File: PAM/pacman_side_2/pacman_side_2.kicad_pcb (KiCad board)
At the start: 2 copper layers, 144.3 x 139.4 mm, 23 parts, among them J1 Conn_01x08, J2 Conn_01x04, J3 Conn_01x01, J4 Conn_01x01, J5 Conn_01x01, J6 Conn_01x02, J9 JST PH, K1 G2RL, K2 G5V-1, K3 G5V-1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

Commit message: finish layout and labeling
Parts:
- added G***: LOGO, AERO_Footprints:AERO_Logo_10x4mm, F.Cu at (112.1, 121.2)
- added REF**: Symbol_HighVoltage_Type2_CopperTop_VerySmall, Symbol:Symbol_HighVoltage_Type2_CopperTop_VerySmall, F.Cu at (163.2, 112.5)
- moved J9 68.9 mm to (107.1, 84.8)
- moved J5 68.1 mm to (137.0, 120.9), turned to 180 degrees
- moved F3 66.9 mm to (103.4, 77.5)
- moved J2 66.9 mm to (95.0, 90.8)
- moved K3 66.9 mm to (98.0, 75.3)
- moved D3 66.9 mm to (126.8, 73.3)
- moved D4 66.9 mm to (114.8, 87.8)
- moved D5 66.9 mm to (121.8, 92.1)
- moved J3 66.9 mm to (176.1, 122.3)
- moved J6 66.9 mm to (117.3, 70.8)
- moved K1 66.9 mm to (143.2, 73.8)
- moved K2 66.9 mm to (112.2, 82.4)
- moved Q2 66.9 mm to (122.6, 83.0)
- moved J1 66.9 mm to (111.3, 111.1)
- moved F1 66.9 mm to (139.0, 85.3)
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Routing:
- net +12V: track 0.00 -> 114.5 mm
- net /BMS_FAN: track 0.00 -> 65.8 mm
- net /INT-: track 0.00 -> 48.5 mm
- net Net-(K1-Pad5): track 0.00 -> 42.9 mm
- net /INT+: track 0.00 -> 35.5 mm
- net /B+: track 0.00 -> 16.3 mm
- net Net-(D1-Pad2): track 0.00 -> 12.1 mm
- net /FAN_OUT: track 3.40 -> 14.8 mm
- net Net-(F1-Pad1): track 0.00 -> 10.9 mm
- net /BMS_CAN-: track 22.9 -> 31.8 mm
- net Net-(F2-Pad1): track 0.00 -> 7.87 mm
- net /BMS_CAN+: track 25.1 -> 31.8 mm
- net /AIR_B+: track 21.9 -> 18.7 mm
- net /AIR_B-: track 76.1 -> 73.4 mm
- net GND: vias 0 -> 3
- added copper zone on B.Cu, net GND
- added copper zone on F.Cu, net GND
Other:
- board size 144.3 x 139.4 mm -> 92.7 x 66 mm
- board text added: "+ -"
- board text added: "12V"
- board text added: "2A"
- board text added: "AIR B+"
- board text added: "AIR B-"
- board text added: "CAN+"
- board text added: "CAN-"
- board text added: "FAN"
- board text added: "GND"
- board text added: "Pack 2"

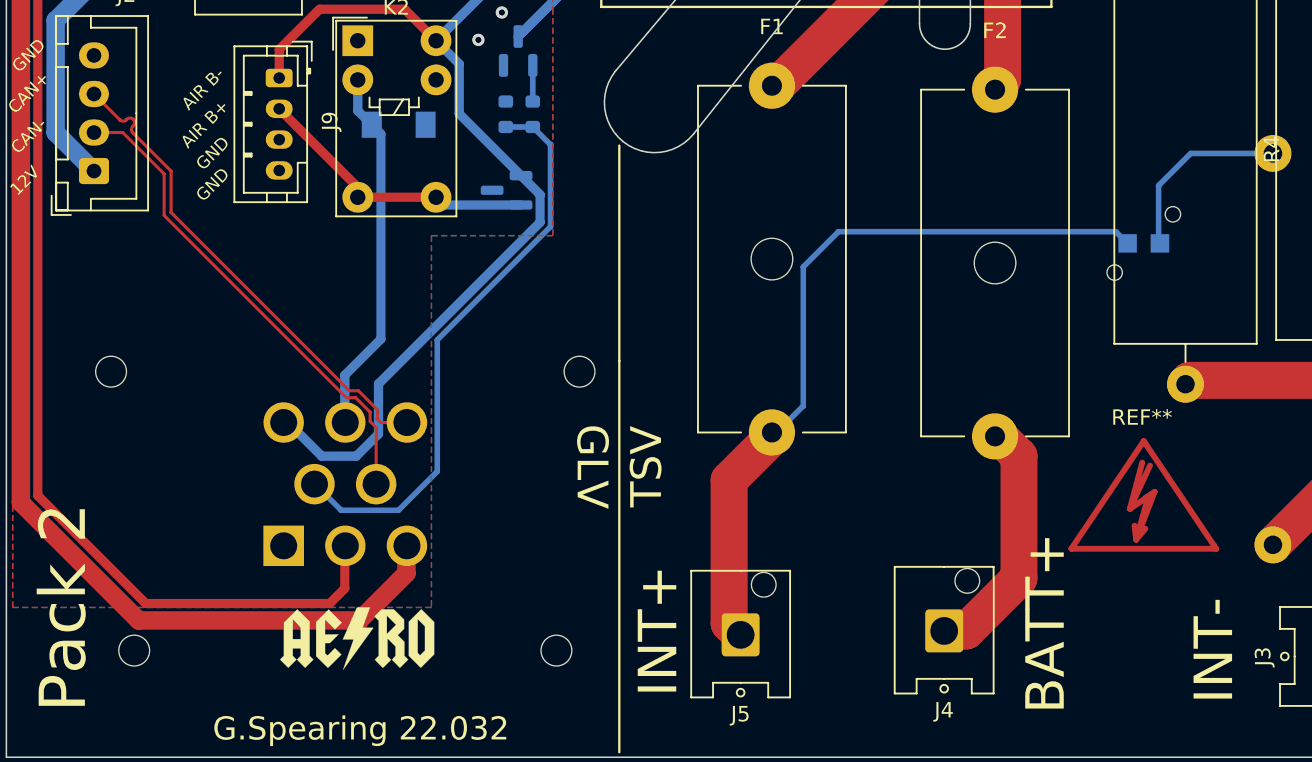
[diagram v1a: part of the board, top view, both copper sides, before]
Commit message: Adding CAN termination resistors
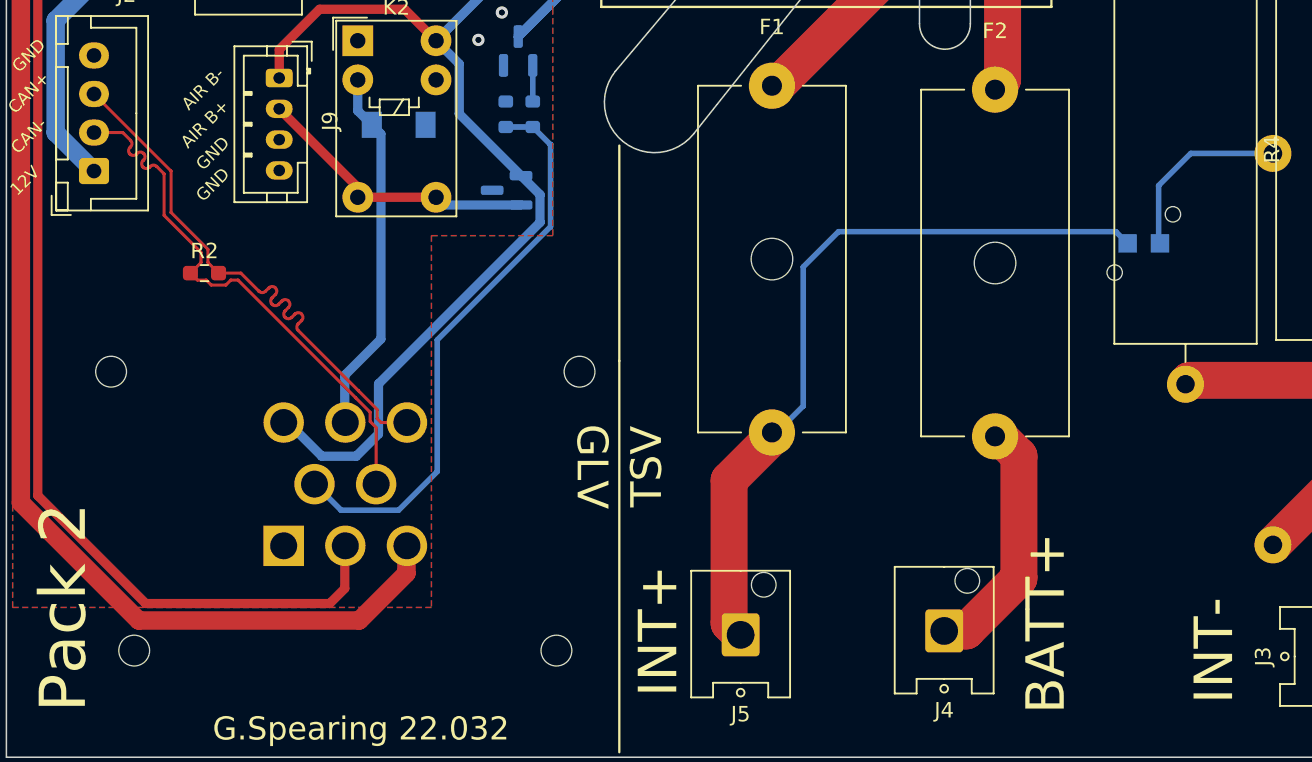
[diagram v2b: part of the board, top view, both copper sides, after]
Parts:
- removed G***: LOGO, AERO_Footprints:AERO_Logo_10x4mm
- removed REF**: Symbol_HighVoltage_Type2_CopperTop_VerySmall, Symbol:Symbol_HighVoltage_Type2_CopperTop_VerySmall
- added R2: 120, Resistor_SMD:R_0603_1608Metric_Pad0.98x0.95mm_HandSolder, F.Cu at (102.2, 97.4)
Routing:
- net /BMS_CAN+: track 31.8 -> 35.4 mm
- net /BMS_CAN-: track 31.8 -> 35.3 mm

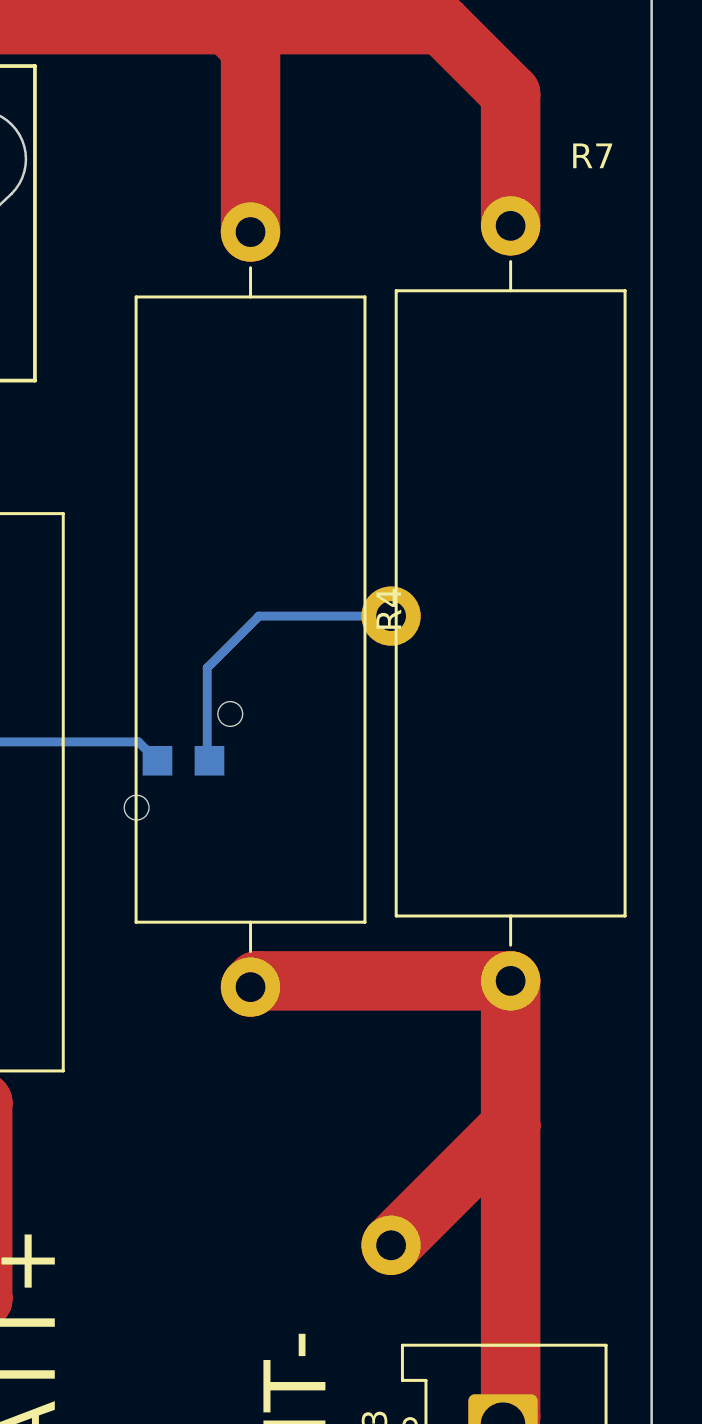
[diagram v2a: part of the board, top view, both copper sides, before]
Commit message: updating silkscreen objects
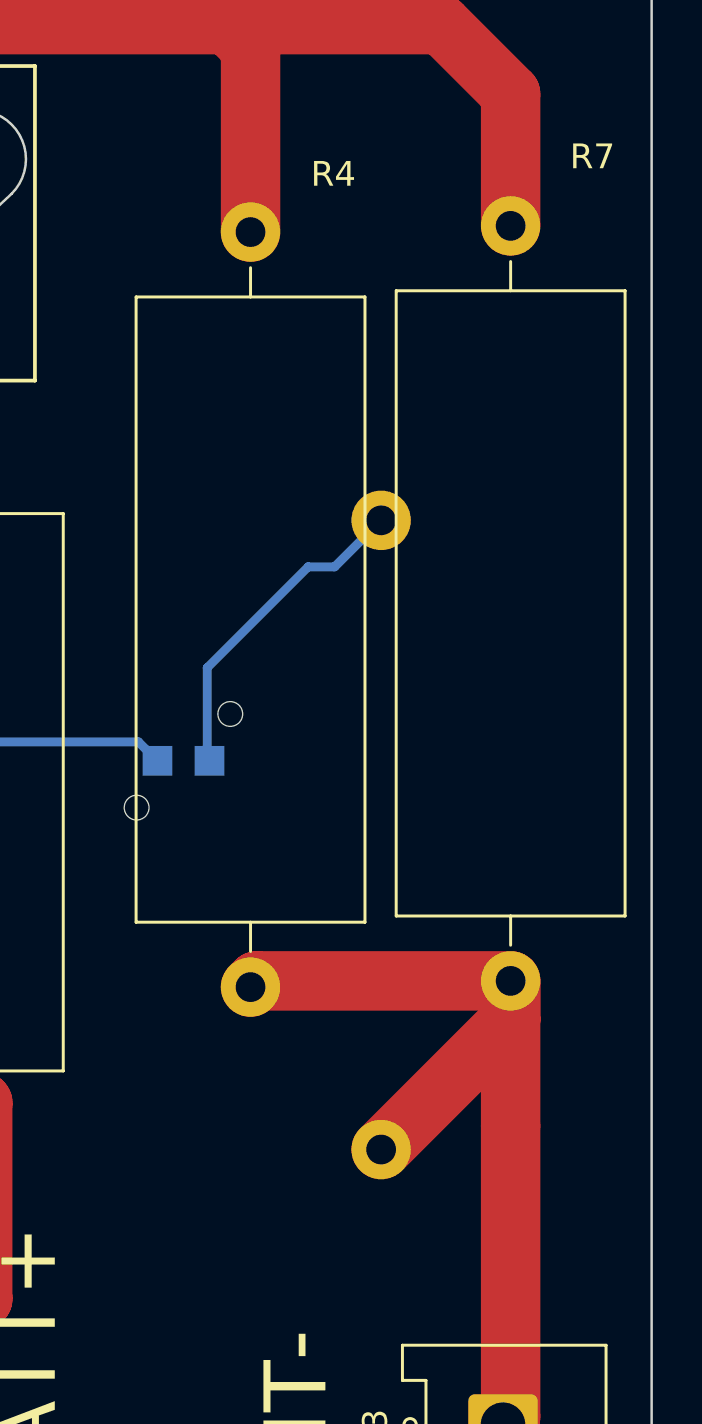
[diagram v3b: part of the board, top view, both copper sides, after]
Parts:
- moved R1 3.89 mm to (171.1, 111.2)
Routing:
- net /INT+: track 35.5 -> 37.6 mm
- net Net-(D1-Pad2): track 12.1 -> 13.3 mm
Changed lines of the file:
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@@
     (property "Sheetname" "")
     (attr through_hole)
-    (fp_text reference "R4" (at 15.24 -5.62 90) (layer "F.SilkS")
+    (fp_text reference "R4" (at -2.3328 -3.3418 180) (layer "F.SilkS")
       (effects (font (size 1 1) (thickness 0.15)))
     )
@@
   )
   (footprint "Resistor_THT:R_Axial_DIN0414_L11.9mm_D4.5mm_P25.40mm_Horizontal" (layer "B.Cu")
-    (at 171.547 115.067 90)
+    (at 171.1452 111.2012 90)
     (descr "Resistor, Axial_DIN0414 series, Axial, Horizontal, pin pitch=25.4mm, 2W, length*diameter=11.9*4.5mm^2, http://www.vishay.com/docs/20128/wkxwrx.pdf")
     (tags "Resistor Axial_DIN0414 series Axial Horizontal pin pitch 25.4mm 2W length 11.9mm diameter 4.5mm")
@@
   (segment (start 162.115 95.509) (end 161.351479 94.745479) (width 0.36) (layer "B.Cu") (net 1))
   (segment (start 161.351479 94.745479) (end 143.354521 94.745479) (width 0.36) (layer "B.Cu") (net 1))
-  (segment (start 171.547 89.667) (end 166.213 89.667) (width 0.36) (layer "B.Cu") (net 2))
-  (segment (start 166.213 89.667) (end 164.125479 91.754521) (width 0.36) (layer "B.Cu") (net 2))
-  (segment (start 164.125479 95.419479) (end 164.215 95.509) (width 0.36) (layer "B.Cu") (net 2))
-  (segment (start 164.125479 91.754521) (end 164.125479 95.419479) (width 0.36) (layer "B.Cu") (net 2))
+  (segment (start 168.1988 87.6812) (end 168.1988 87.6808) (width 0.36) (layer "B.Cu") (net 2))
+  (segment (start 164.125479 91.754521) (end 168.1988 87.6812) (width 0.36) (layer "B.Cu") (net 2))
+  (segment (start 164.125479 95.419479) (end 164.125479 91.754521) (width 0.36) (layer "B.Cu") (net 2))
+  (segment (start 164.215 95.509) (end 164.125479 95.419479) (width 0.36) (layer "B.Cu") (net 2))
+  (segment (start 168.1988 87.6808) (end 169.2656 87.6808) (width 0.36) (layer "B.Cu") (net 2))
+  (segment (start 169.2656 87.6808) (end 171.1452 85.8012) (width 0.36) (layer "B.Cu") (net 2))
   (segment (start 127.02531 77.621) (end 130.5 77.621) (width 0.6) (layer "B.Cu") (net 3))
   (segment (start 122.565 82.08131) (end 127.02531 77.621) (width 0.6) (layer "B.Cu") (net 3))
@@
   (arc (start 107.018965 99.459581) (mid 106.806833 99.547449) (end 106.594701 99.459581) (width 0.2) (layer "F.Cu") (net 14))
   (segment (start 176.373 122.003) (end 176.065 122.311) (width 2.4) (layer "F.Cu") (net 15))
+  (segment (start 176.373 105.9734) (end 171.1452 111.2012) (width 2.4) (layer "F.Cu") (net 15))
   (segment (start 176.373 104.394) (end 166.123 104.394) (width 2.4) (layer "F.Cu") (net 15))
   (segment (start 166.123 104.394) (end 165.873 104.644) (width 2.4) (layer "F.Cu") (net 15))
   (segment (start 176.373 110.241) (end 176.373 122.003) (width 2.4) (layer "F.Cu") (net 15))
   (segment (start 176.373 104.394) (end 176.373 110.241) (width 2.4) (layer "F.Cu") (net 15))
-  (segment (start 176.373 110.241) (end 171.547 115.067) (width 2.4) (layer "F.Cu") (net 15))
+  (segment (start 176.373 104.394) (end 176.373 105.9734) (width 2.4) (layer "F.Cu") (net 15))
   (segment (start 165.873 66.721) (end 165.873 74.164) (width 2.4) (layer "F.Cu") (net 16))
   (segment (start 154.83 65.791) (end 164.943 65.791) (width 2.4) (layer "F.Cu") (net 16))

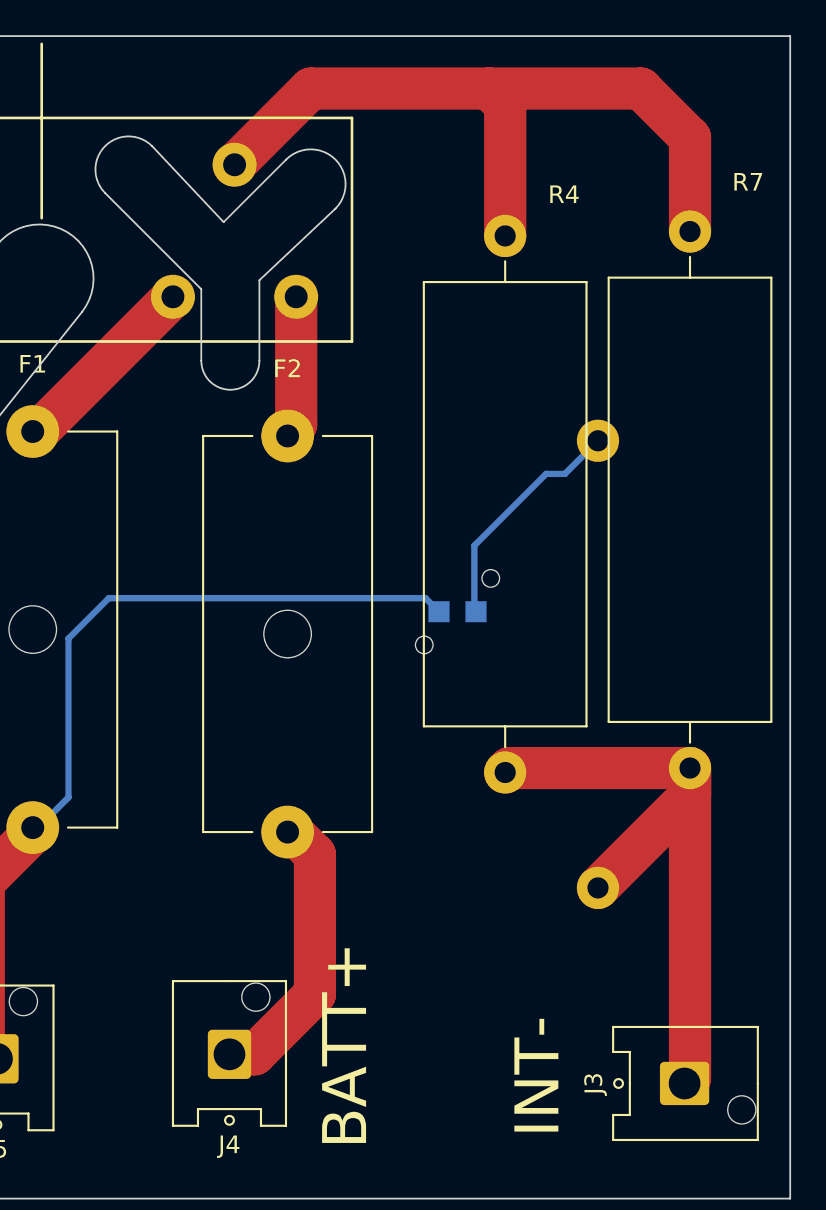
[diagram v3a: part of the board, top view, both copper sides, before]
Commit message: Major Review and Part Update
updating footprints, component values, layouts
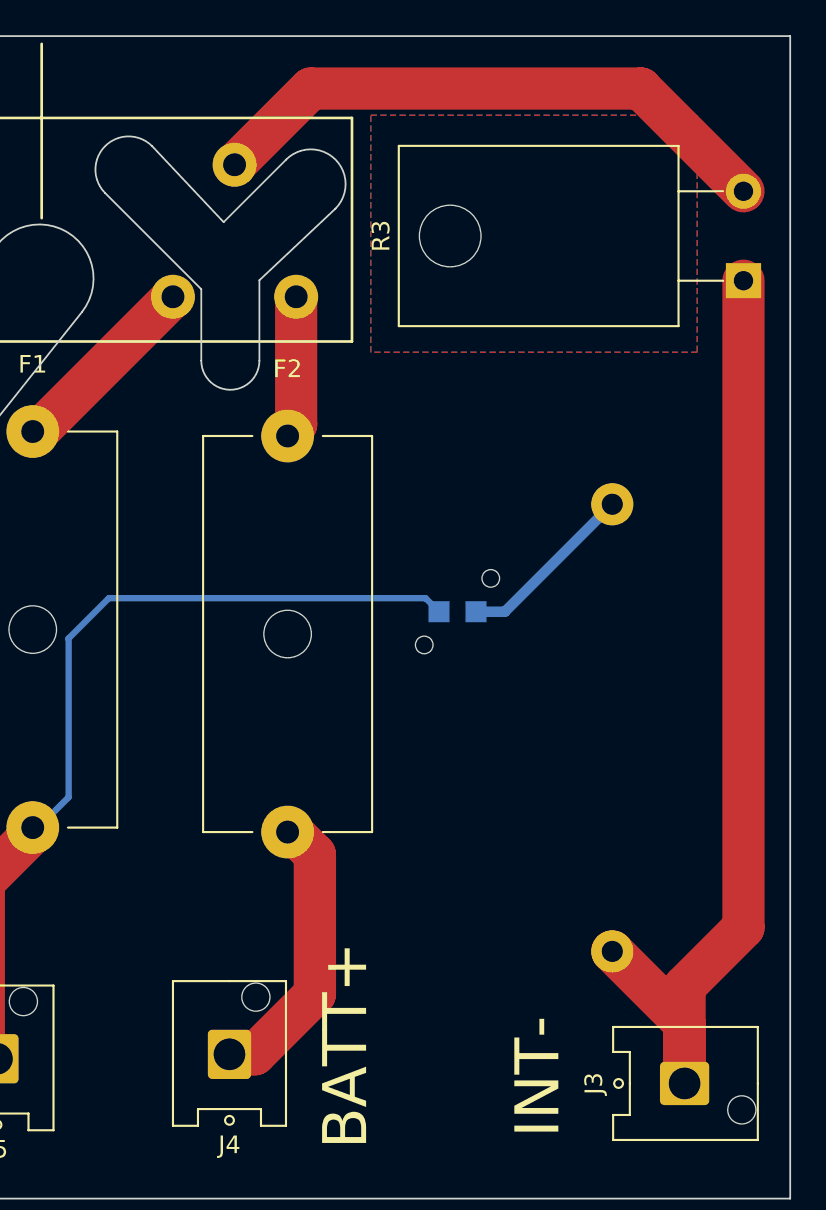
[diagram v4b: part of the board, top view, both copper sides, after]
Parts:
- removed R4, R7: 1k 7W, Resistor_THT:R_Axial_Power_L25.0mm_W9.0mm_P30.48mm
- added R3: 500, Package_TO_SOT_THT:TO-220-2_Horizontal_TabDown, F.Cu at (179.4, 76.7)
- moved R1 3.70 mm to (172.0, 114.8)
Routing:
- net /INT+: track 37.6 -> 56.2 mm
- net Net-(K1-Pad5): track 42.9 -> 33.1 mm
- net Net-(D1-Pad2): track 13.3 -> 10.3 mm
- added copper zone on B.Cu, net (none)
- added copper zone on F.Cu, net (none)

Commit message: touching up layout and making gerbers
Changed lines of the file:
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@@
       (outputformat 1)
       (mirror false)
-      (drillshape 1)
+      (drillshape 0)
       (scaleselection 1)
-      (outputdirectory "")
+      (outputdirectory "Pac2_Gerber/")
     )
   )
@@
     (fp_line (start 7.95 -1.7) (end -1.95 -1.7) (layer "F.Fab") (width 0.1))
     (fp_line (start 7.95 2.8) (end 7.95 -1.7) (layer "F.Fab") (width 0.1))
-    (pad "1" thru_hole roundrect locked (at 0 0 270) (size 1.2 1.75) (drill 0.75) (layers *.Cu *.Mask) (roundrect_rratio 0.208333)
+    (pad "1" thru_hole roundrect locked (at 0 0 270) (size 1.2 1.75) (drill 0.75) (layers *.Cu *.Mask) (roundrect_rratio 0.2083333333)
       (net 12 "/AIR_B-") (pinfunction "Pin_1") (pintype "passive"))
     (pad "2" thru_hole oval locked (at 2 0 270) (size 1.2 1.75) (drill 0.75) (layers *.Cu *.Mask)
@@
     (fp_line (start 0 -1.35) (end 0.625 -2.35) (layer "F.Fab") (width 0.1))
     (fp_line (start 9.95 -2.35) (end -2.45 -2.35) (layer "F.Fab") (width 0.1))
-    (pad "1" thru_hole roundrect locked (at 0 0 90) (size 1.7 1.95) (drill 0.95) (layers *.Cu *.Mask) (roundrect_rratio 0.147059)
+    (pad "1" thru_hole roundrect locked (at 0 0 90) (size 1.7 1.95) (drill 0.95) (layers *.Cu *.Mask) (roundrect_rratio 0.1470588235)
       (net 10 "+12V") (pinfunction "Pin_1") (pintype "passive"))
     (pad "2" thru_hole oval locked (at 2.5 0 90) (size 1.7 1.95) (drill 0.95) (layers *.Cu *.Mask)
@@
     (fp_line (start -3.1 4.05) (end -3.1 -3.95) (layer "F.Fab") (width 0.1))
     (pad "" np_thru_hole circle locked (at -1.5 3.25 90) (size 1.6 1.6) (drill 1.6) (layers *.Cu *.Mask))
-    (pad "1" thru_hole roundrect locked (at 0 0 90) (size 2.46 2.8) (drill 1.8) (layers *.Cu *.Mask) (roundrect_rratio 0.101626)
+    (pad "1" thru_hole roundrect locked (at 0 0 90) (size 2.46 2.8) (drill 1.8) (layers *.Cu *.Mask) (roundrect_rratio 0.1016260163)
       (net 15 "/INT+") (pinfunction "Pin_1") (pintype "passive"))
     (model "${KICAD6_3DMODEL_DIR}/Connector_Hirose.3dshapes/Hirose_DF63M-1P-3.96DSA_1x01_P3.96mm_Vertical.wrl"
@@
     (fp_line (start 4.95 -2.35) (end -2.45 -2.35) (layer "F.Fab") (width 0.1))
     (fp_line (start 0 -1.35) (end 0.625 -2.35) (layer "F.Fab") (width 0.1))
-    (pad "1" thru_hole roundrect locked (at 0 0 270) (size 1.7 2) (drill 1) (layers *.Cu *.Mask) (roundrect_rratio 0.147059)
+    (pad "1" thru_hole roundrect locked (at 0 0 270) (size 1.7 2) (drill 1) (layers *.Cu *.Mask) (roundrect_rratio 0.1470588235)
       (net 19 "Net-(F3-Pad2)") (pinfunction "Pin_1") (pintype "passive"))
     (pad "2" thru_hole oval locked (at 2.5 0 270) (size 1.7 2) (drill 1) (layers *.Cu *.Mask)
@@
     (fp_line (start -3.1 -3.95) (end -1.9 -3.95) (layer "F.Fab") (width 0.1))
     (pad "" np_thru_hole circle locked (at -1.5 3.25 180) (size 1.6 1.6) (drill 1.6) (layers *.Cu *.Mask))
-    (pad "1" thru_hole roundrect locked (at 0 0 180) (size 2.46 2.8) (drill 1.8) (layers *.Cu *.Mask) (roundrect_rratio 0.101626)
+    (pad "1" thru_hole roundrect locked (at 0 0 180) (size 2.46 2.8) (drill 1.8) (layers *.Cu *.Mask) (roundrect_rratio 0.1016260163)
       (net 9 "/B+") (pinfunction "Pin_1") (pintype "passive"))
     (model "${KICAD6_3DMODEL_DIR}/Connector_Hirose.3dshapes/Hirose_DF63M-1P-3.96DSA_1x01_P3.96mm_Vertical.wrl"
@@
     (fp_line (start 3.1 -3.95) (end 1.9 -3.95) (layer "F.Fab") (width 0.1))
     (pad "" np_thru_hole circle locked (at -1.5 3.25 180) (size 1.6 1.6) (drill 1.6) (layers *.Cu *.Mask))
-    (pad "1" thru_hole roundrect locked (at 0 0 180) (size 2.46 2.8) (drill 1.8) (layers *.Cu *.Mask) (roundrect_rratio 0.101626)
+    (pad "1" thru_hole roundrect locked (at 0 0 180) (size 2.46 2.8) (drill 1.8) (layers *.Cu *.Mask) (roundrect_rratio 0.1016260163)
       (net 1 "/INT-") (pinfunction "Pin_1") (pintype "passive"))
     (model "${KICAD6_3DMODEL_DIR}/Connector_Hirose.3dshapes/Hirose_DF63M-1P-3.96DSA_1x01_P3.96mm_Vertical.wrl"
